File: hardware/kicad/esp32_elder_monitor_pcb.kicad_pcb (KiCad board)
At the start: 2 copper layers, 100 x 80 mm, 16 parts, among them J1 ESP32_LEFT, J10 FSR402, J11 SW420, J12 SOS_BTN, J13 BUZZER, J14 FAN_RELAY, J15 LED_LIGHT, J16 SERVO, J2 SPARE_GPIO, J3 5V_IN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

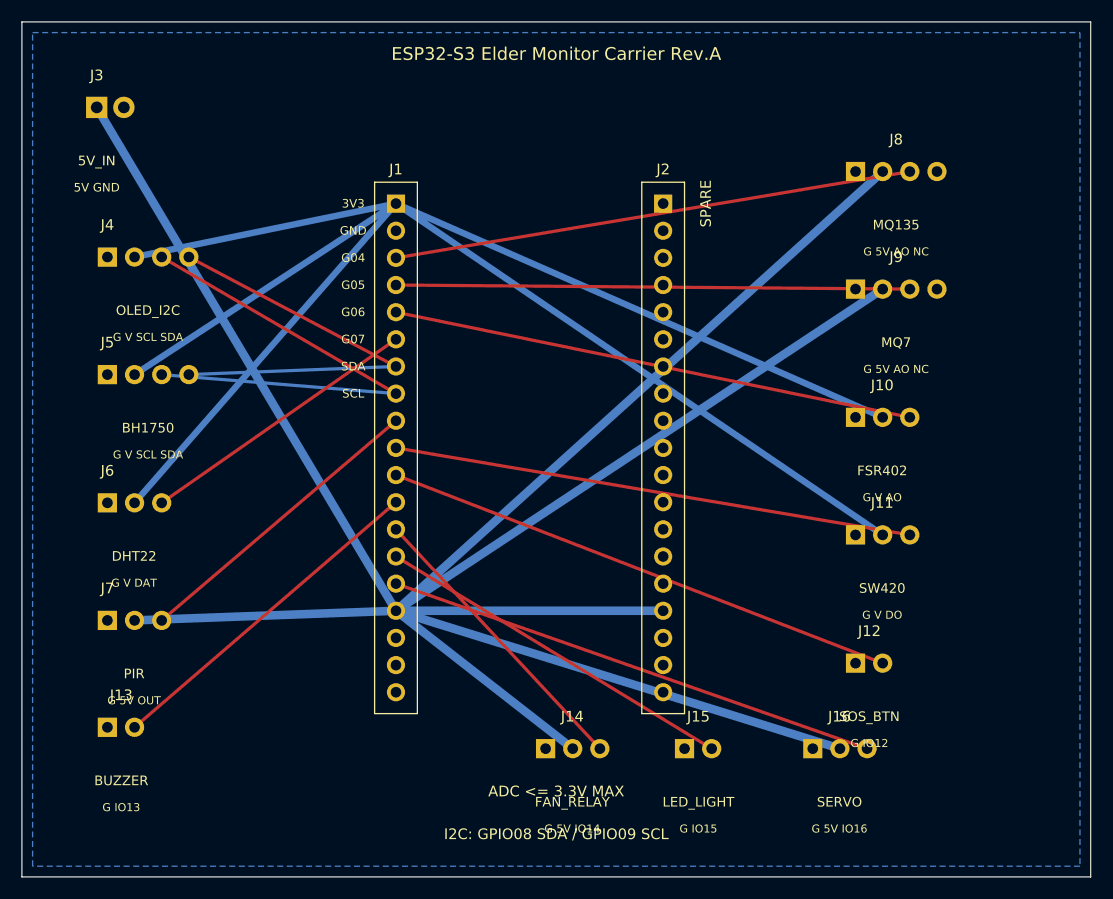
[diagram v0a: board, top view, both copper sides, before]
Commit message: Update ESP32 PCB layout dimensions
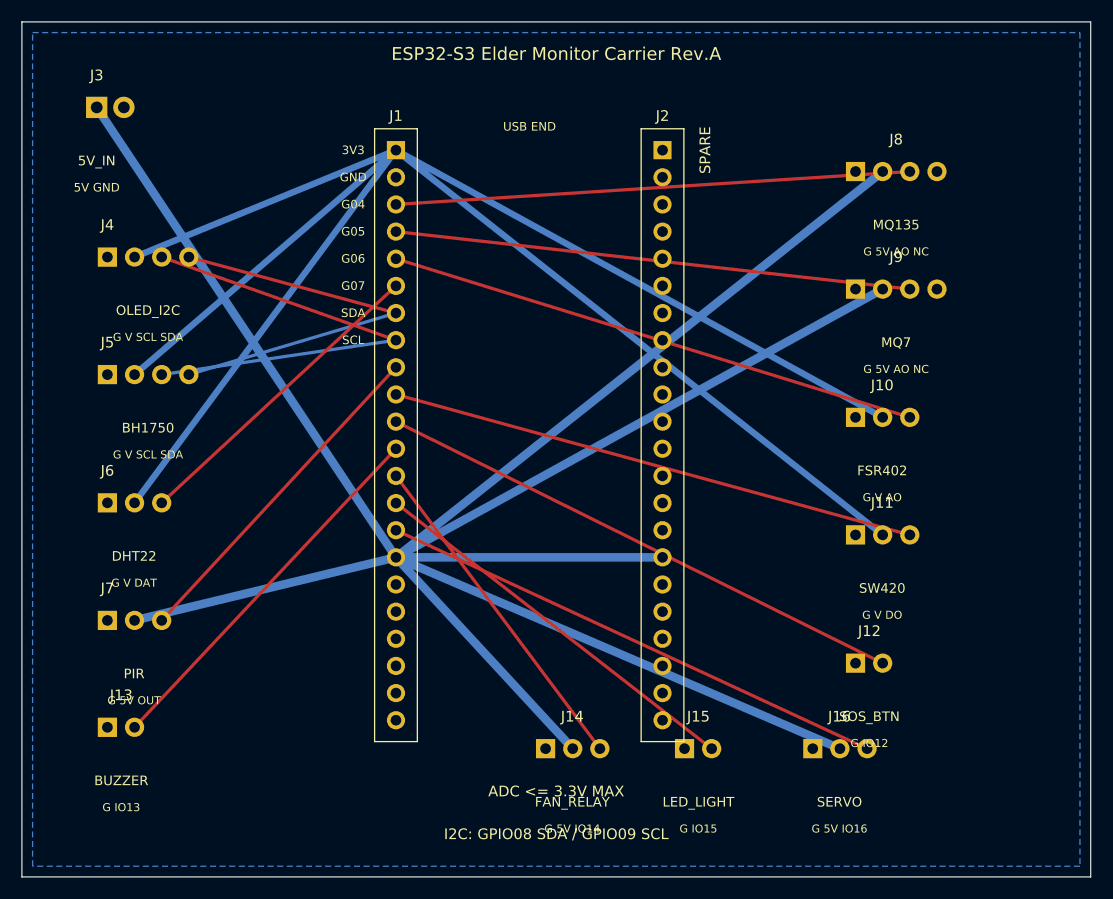
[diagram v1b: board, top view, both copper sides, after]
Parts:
- J1: value ESP32_LEFT -> ESP32_LEFT_22P
- J2: value SPARE_GPIO -> SPARE_GPIO_22P
- moved J2 5.00 mm to (69.9, 22.0)
- moved J1 5.00 mm to (45.0, 22.0)
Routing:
- net +3V3: track 196.2 -> 209.7 mm
- net +5V: track 284.7 -> 280.4 mm
- net GPIO14_FAN: track 28.0 -> 31.9 mm
- net GPIO10_PIR: track 28.8 -> 32.3 mm
- net GPIO13_BUZZER: track 32.3 -> 35.7 mm
- net GPIO07_DHT22: track 26.7 -> 29.9 mm
- net GPIO15_LED: track 34.6 -> 37.4 mm
- net GPIO12_SOS: track 48.8 -> 50.8 mm
- net GPIO09_SCL: track 47.4 -> 45.4 mm
- net GPIO16_SERVO: track 46.7 -> 48.6 mm
- net GPIO06_FSR: track 49.1 -> 50.3 mm
- net GPIO11_SW420: track 48.8 -> 49.8 mm
- net GPIO08_SDA: track 41.3 -> 40.3 mm
- net GPIO04_MQ135: track 48.8 -> 48.2 mm
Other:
- board text added: "ESP32-S3 module outline ref: 22P x2, row pitch 24.94mm"
- board text added: "USB END"
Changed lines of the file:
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@@
   (gr_text "I2C: GPIO08 SDA / GPIO09 SCL" (at 60 86) (layer "F.SilkS") (effects (font (size 1 1) (thickness 0.15))))
   (gr_text "ADC <= 3.3V MAX" (at 60 82) (layer "F.SilkS") (effects (font (size 1 1) (thickness 0.15))))
+  (gr_rect (start 39 18) (end 76 81) (layer "Dwgs.User") (width 0.15))
+  (gr_text "ESP32-S3 module outline ref: 22P x2, row pitch 24.94mm" (at 57.5 16.5) (layer "Dwgs.User") (effects (font (size 0.9 0.9) (thickness 0.12))))
+  (gr_text "USB END" (at 57.5 19.8) (layer "F.SilkS") (effects (font (size 0.8 0.8) (thickness 0.12))))
   (footprint "Local:ESP32-S3_DEVKIT_SOCKET_LEFT" (layer "F.Cu")
-    (at 45 27)
-    (descr "ESP32-S3 DevKit left 1x19 socket, 2.54mm")
+    (at 45 22)
+    (descr "ESP32-S3 DevKit left 1x22 socket, 2.54mm pitch, row pitch 24.94mm from provided PDF")
     (property "Reference" "J1" (at 0 -3.2 0) (layer "F.SilkS") (effects (font (size 1 1) (thickness 0.15))))
-    (property "Value" "ESP32_LEFT" (at 0 49 0) (layer "F.Fab") (effects (font (size 1 1) (thickness 0.15))))
+    (property "Value" "ESP32_LEFT_22P" (at 0 56.5 0) (layer "F.Fab") (effects (font (size 1 1) (thickness 0.15))))
     (fp_text user "3V3" (at -4 0 0) (layer "F.SilkS") (effects (font (size 0.8 0.8) (thickness 0.12))))
     (fp_text user "GND" (at -4 2.54 0) (layer "F.SilkS") (effects (font (size 0.8 0.8) (thickness 0.12))))
@@
     (fp_text user "SCL" (at -4 17.78 0) (layer "F.SilkS") (effects (font (size 0.8 0.8) (thickness 0.12))))
     (fp_line (start -2 -2) (end 2 -2) (layer "F.SilkS") (width 0.12))
-    (fp_line (start 2 -2) (end 2 47.72) (layer "F.SilkS") (width 0.12))
-    (fp_line (start 2 47.72) (end -2 47.72) (layer "F.SilkS") (width 0.12))
-    (fp_line (start -2 47.72) (end -2 -2) (layer "F.SilkS") (width 0.12))
+    (fp_line (start 2 -2) (end 2 55.34) (layer "F.SilkS") (width 0.12))
+    (fp_line (start 2 55.34) (end -2 55.34) (layer "F.SilkS") (width 0.12))
+    (fp_line (start -2 55.34) (end -2 -2) (layer "F.SilkS") (width 0.12))
     (pad "1" thru_hole rect (at 0 0) (size 1.7 1.7) (drill 1.0) (layers "*.Cu" "*.Mask") (net 2 "+3V3"))
     (pad "2" thru_hole oval (at 0 2.54) (size 1.7 1.7) (drill 1.0) (layers "*.Cu" "*.Mask") (net 1 "GND"))
@@
     (pad "18" thru_hole oval (at 0 43.18) (size 1.7 1.7) (drill 1.0) (layers "*.Cu" "*.Mask") (net 17 "NC"))
     (pad "19" thru_hole oval (at 0 45.72) (size 1.7 1.7) (drill 1.0) (layers "*.Cu" "*.Mask") (net 17 "NC"))
+    (pad "20" thru_hole oval (at 0 48.26) (size 1.7 1.7) (drill 1.0) (layers "*.Cu" "*.Mask") (net 17 "NC"))
+    (pad "21" thru_hole oval (at 0 50.8) (size 1.7 1.7) (drill 1.0) (layers "*.Cu" "*.Mask") (net 17 "NC"))
+    (pad "22" thru_hole oval (at 0 53.34) (size 1.7 1.7) (drill 1.0) (layers "*.Cu" "*.Mask") (net 17 "NC"))
   )
   (footprint "Local:ESP32-S3_DEVKIT_SOCKET_RIGHT" (layer "F.Cu")
-    (at 70 27)
-    (descr "ESP32-S3 DevKit right 1x19 socket, spare breakout")
+    (at 69.94 22)
+    (descr "ESP32-S3 DevKit right 1x22 socket, spare breakout")
     (property "Reference" "J2" (at 0 -3.2 0) (layer "F.SilkS") (effects (font (size 1 1) (thickness 0.15))))
-    (property "Value" "SPARE_GPIO" (at 0 49 0) (layer "F.Fab") (effects (font (size 1 1) (thickness 0.15))))
+    (property "Value" "SPARE_GPIO_22P" (at 0 56.5 0) (layer "F.Fab") (effects (font (size 1 1) (thickness 0.15))))
     (fp_text user "SPARE" (at 4 0 90) (layer "F.SilkS") (effects (font (size 1 1) (thickness 0.15))))
     (fp_line (start -2 -2) (end 2 -2) (layer "F.SilkS") (width 0.12))
-    (fp_line (start 2 -2) (end 2 47.72) (layer "F.SilkS") (width 0.12))
-    (fp_line (start 2 47.72) (end -2 47.72) (layer "F.SilkS") (width 0.12))
-    (fp_line (start -2 47.72) (end -2 -2) (layer "F.SilkS") (width 0.12))
+    (fp_line (start 2 -2) (end 2 55.34) (layer "F.SilkS") (width 0.12))
+    (fp_line (start 2 55.34) (end -2 55.34) (layer "F.SilkS") (width 0.12))
+    (fp_line (start -2 55.34) (end -2 -2) (layer "F.SilkS") (width 0.12))
     (pad "1" thru_hole rect (at 0 0) (size 1.7 1.7) (drill 1.0) (layers "*.Cu" "*.Mask") (net 2 "+3V3"))
     (pad "2" thru_hole oval (at 0 2.54) (size 1.7 1.7) (drill 1.0) (layers "*.Cu" "*.Mask") (net 1 "GND"))
@@
     (pad "18" thru_hole oval (at 0 43.18) (size 1.7 1.7) (drill 1.0) (layers "*.Cu" "*.Mask") (net 17 "NC"))
     (pad "19" thru_hole oval (at 0 45.72) (size 1.7 1.7) (drill 1.0) (layers "*.Cu" "*.Mask") (net 17 "NC"))
+    (pad "20" thru_hole oval (at 0 48.26) (size 1.7 1.7) (drill 1.0) (layers "*.Cu" "*.Mask") (net 17 "NC"))
+    (pad "21" thru_hole oval (at 0 50.8) (size 1.7 1.7) (drill 1.0) (layers "*.Cu" "*.Mask") (net 17 "NC"))
+    (pad "22" thru_hole oval (at 0 53.34) (size 1.7 1.7) (drill 1.0) (layers "*.Cu" "*.Mask") (net 17 "NC"))
   )
   (footprint "Local:HEADER_1X02_PWR" (layer "F.Cu")
@@
     (pad "3" thru_hole oval (at 5.08 0) (size 1.8 1.8) (drill 1.0) (layers "*.Cu" "*.Mask") (net 16 "GPIO16_SERVO"))
   )
-  (segment (start 45 42.24) (end 25.62 32) (width 0.3) (layer "F.Cu") (net 8))
-  (segment (start 45 44.78) (end 23.08 32) (width 0.3) (layer "F.Cu") (net 9))
-  (segment (start 45 42.24) (end 25.62 43) (width 0.3) (layer "B.Cu") (net 8))
-  (segment (start 45 44.78) (end 23.08 43) (width 0.3) (layer "B.Cu") (net 9))
-  (segment (start 45 39.7) (end 23.08 55) (width 0.3) (layer "F.Cu") (net 7))
-  (segment (start 45 47.32) (end 23.08 66) (width 0.3) (layer "F.Cu") (net 10))
-  (segment (start 45 32.08) (end 93.08 24) (width 0.3) (layer "F.Cu") (net 4))
-  (segment (start 45 34.62) (end 93.08 35) (width 0.3) (layer "F.Cu") (net 5))
-  (segment (start 45 37.16) (end 93.08 47) (width 0.3) (layer "F.Cu") (net 6))
-  (segment (start 45 49.86) (end 93.08 58) (width 0.3) (layer "F.Cu") (net 11))
-  (segment (start 45 52.4) (end 90.54 70) (width 0.3) (layer "F.Cu") (net 12))
-  (segment (start 45 54.94) (end 20.54 76) (width 0.3) (layer "F.Cu") (net 13))
-  (segment (start 45 57.48) (end 64.08 78) (width 0.3) (layer "F.Cu") (net 14))
-  (segment (start 45 60.02) (end 74.54 78) (width 0.3) (layer "F.Cu") (net 15))
-  (segment (start 45 62.56) (end 89.08 78) (width 0.3) (layer "F.Cu") (net 16))
-  (segment (start 17 18) (end 45 65.1) (width 0.8) (layer "B.Cu") (net 3))
-  (segment (start 45 65.1) (end 70 65.1) (width 0.8) (layer "B.Cu") (net 3))
-  (segment (start 20.54 66) (end 45 65.1) (width 0.8) (layer "B.Cu") (net 3))
-  (segment (start 90.54 24) (end 45 65.1) (width 0.8) (layer "B.Cu") (net 3))
-  (segment (start 90.54 35) (end 45 65.1) (width 0.8) (layer "B.Cu") (net 3))
-  (segment (start 61.54 78) (end 45 65.1) (width 0.8) (layer "B.Cu") (net 3))
-  (segment (start 86.54 78) (end 45 65.1) (width 0.8) (layer "B.Cu") (net 3))
-  (segment (start 45 27) (end 20.54 32) (width 0.6) (layer "B.Cu") (net 2))
-  (segment (start 45 27) (end 20.54 43) (width 0.6) (layer "B.Cu") (net 2))
-  (segment (start 45 27) (end 20.54 55) (width 0.6) (layer "B.Cu") (net 2))
-  (segment (start 45 27) (end 90.54 47) (width 0.6) (layer "B.Cu") (net 2))
-  (segment (start 45 27) (end 90.54 58) (width 0.6) (layer "B.Cu") (net 2))
+  (segment (start 45 37.24) (end 25.62 32) (width 0.3) (layer "F.Cu") (net 8))
+  (segment (start 45 39.78) (end 23.08 32) (width 0.3) (layer "F.Cu") (net 9))
+  (segment (start 45 37.24) (end 25.62 43) (width 0.3) (layer "B.Cu") (net 8))
+  (segment (start 45 39.78) (end 23.08 43) (width 0.3) (layer "B.Cu") (net 9))
+  (segment (start 45 34.7) (end 23.08 55) (width 0.3) (layer "F.Cu") (net 7))
+  (segment (start 45 42.32) (end 23.08 66) (width 0.3) (layer "F.Cu") (net 10))
+  (segment (start 45 27.08) (end 93.08 24) (width 0.3) (layer "F.Cu") (net 4))
+  (segment (start 45 29.62) (end 93.08 35) (width 0.3) (layer "F.Cu") (net 5))
+  (segment (start 45 32.16) (end 93.08 47) (width 0.3) (layer "F.Cu") (net 6))
+  (segment (start 45 44.86) (end 93.08 58) (width 0.3) (layer "F.Cu") (net 11))
+  (segment (start 45 47.4) (end 90.54 70) (width 0.3) (layer "F.Cu") (net 12))
+  (segment (start 45 49.94) (end 20.54 76) (width 0.3) (layer "F.Cu") (net 13))
+  (segment (start 45 52.48) (end 64.08 78) (width 0.3) (layer "F.Cu") (net 14))
+  (segment (start 45 55.02) (end 74.54 78) (width 0.3) (layer "F.Cu") (net 15))
+  (segment (start 45 57.56) (end 89.08 78) (width 0.3) (layer "F.Cu") (net 16))
+  (segment (start 17 18) (end 45 60.1) (width 0.8) (layer "B.Cu") (net 3))
+  (segment (start 45 60.1) (end 69.94 60.1) (width 0.8) (layer "B.Cu") (net 3))
+  (segment (start 20.54 66) (end 45 60.1) (width 0.8) (layer "B.Cu") (net 3))
+  (segment (start 90.54 24) (end 45 60.1) (width 0.8) (layer "B.Cu") (net 3))
+  (segment (start 90.54 35) (end 45 60.1) (width 0.8) (layer "B.Cu") (net 3))
+  (segment (start 61.54 78) (end 45 60.1) (width 0.8) (layer "B.Cu") (net 3))
+  (segment (start 86.54 78) (end 45 60.1) (width 0.8) (layer "B.Cu") (net 3))
+  (segment (start 45 22) (end 20.54 32) (width 0.6) (layer "B.Cu") (net 2))
+  (segment (start 45 22) (end 20.54 43) (width 0.6) (layer "B.Cu") (net 2))
+  (segment (start 45 22) (end 20.54 55) (width 0.6) (layer "B.Cu") (net 2))
+  (segment (start 45 22) (end 90.54 47) (width 0.6) (layer "B.Cu") (net 2))
+  (segment (start 45 22) (end 90.54 58) (width 0.6) (layer "B.Cu") (net 2))
   (zone (net 1) (net_name "GND") (layer "B.Cu") (hatch edge 0.5)
     (connect_pads (clearance 0.25))

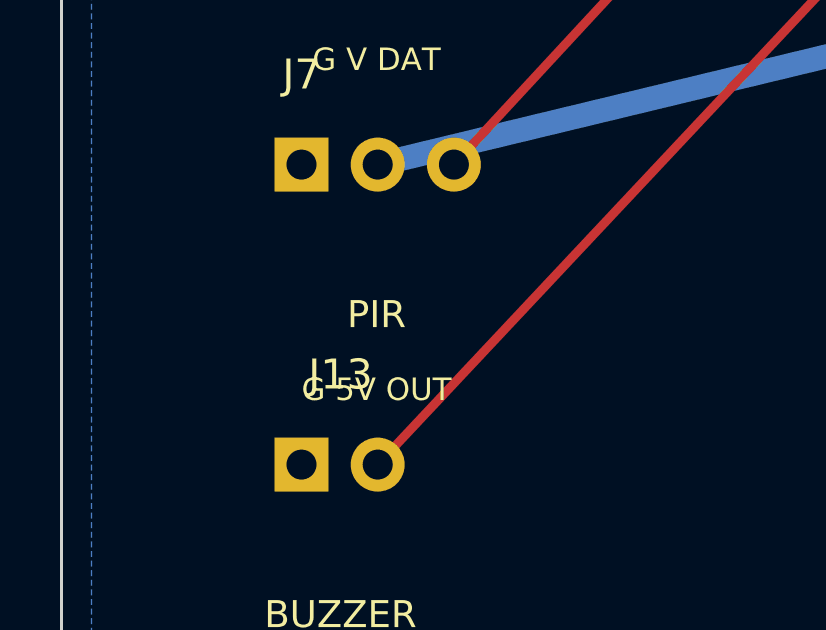
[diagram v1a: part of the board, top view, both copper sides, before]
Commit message: feat: add elder monitor web controls
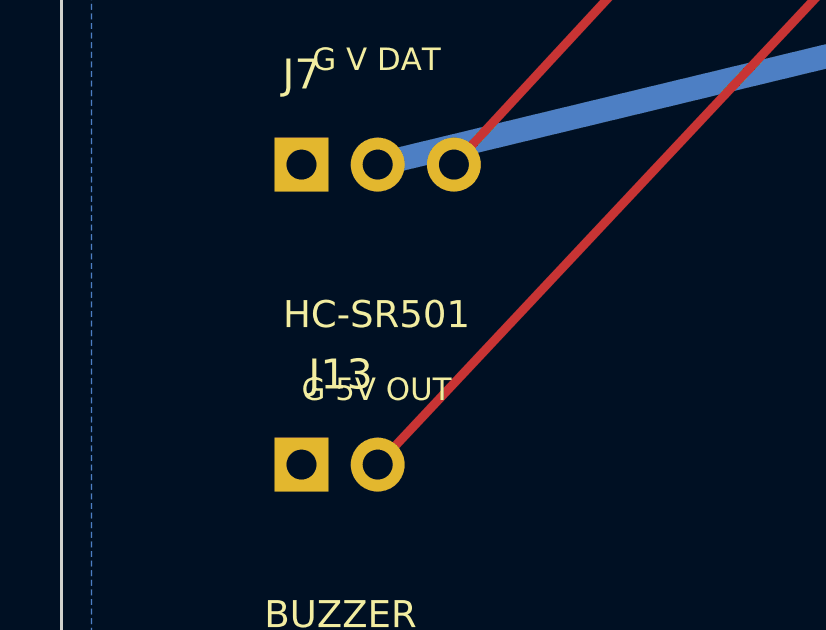
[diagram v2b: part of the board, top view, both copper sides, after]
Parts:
- J7: value PIR -> HC-SR501
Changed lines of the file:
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@@
     (at 18 66)
     (property "Reference" "J7" (at 0 -3 0) (layer "F.SilkS") (effects (font (size 1 1) (thickness 0.15))))
-    (property "Value" "PIR" (at 2.5 5 0) (layer "F.SilkS") (effects (font (size 0.9 0.9) (thickness 0.12))))
+    (property "Value" "HC-SR501" (at 2.5 5 0) (layer "F.SilkS") (effects (font (size 0.9 0.9) (thickness 0.12))))
     (fp_text user "G 5V OUT" (at 2.5 7.5 0) (layer "F.SilkS") (effects (font (size 0.75 0.75) (thickness 0.1))))
     (pad "1" thru_hole rect (at 0 0) (size 1.8 1.8) (drill 1.0) (layers "*.Cu" "*.Mask") (net 1 "GND"))
